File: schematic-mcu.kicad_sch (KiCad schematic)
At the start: 24 parts, among them U5 USBLC6-2P6, U6 ESP32-S3FN8, Y1 Crystal_GND24

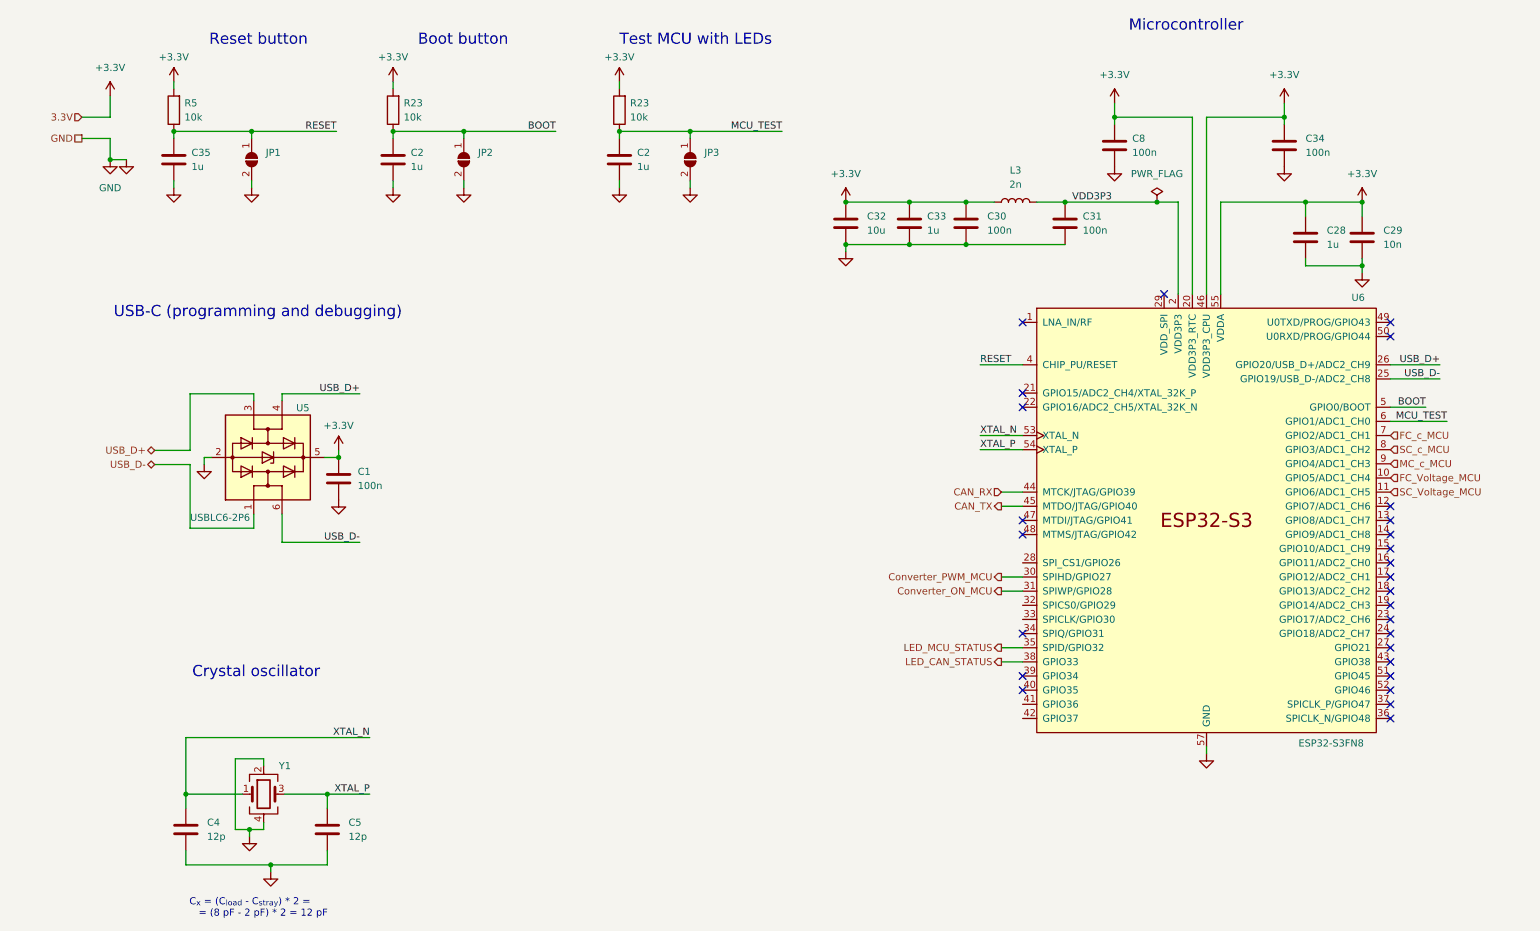
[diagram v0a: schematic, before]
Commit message: Add footprints, Placing MCU
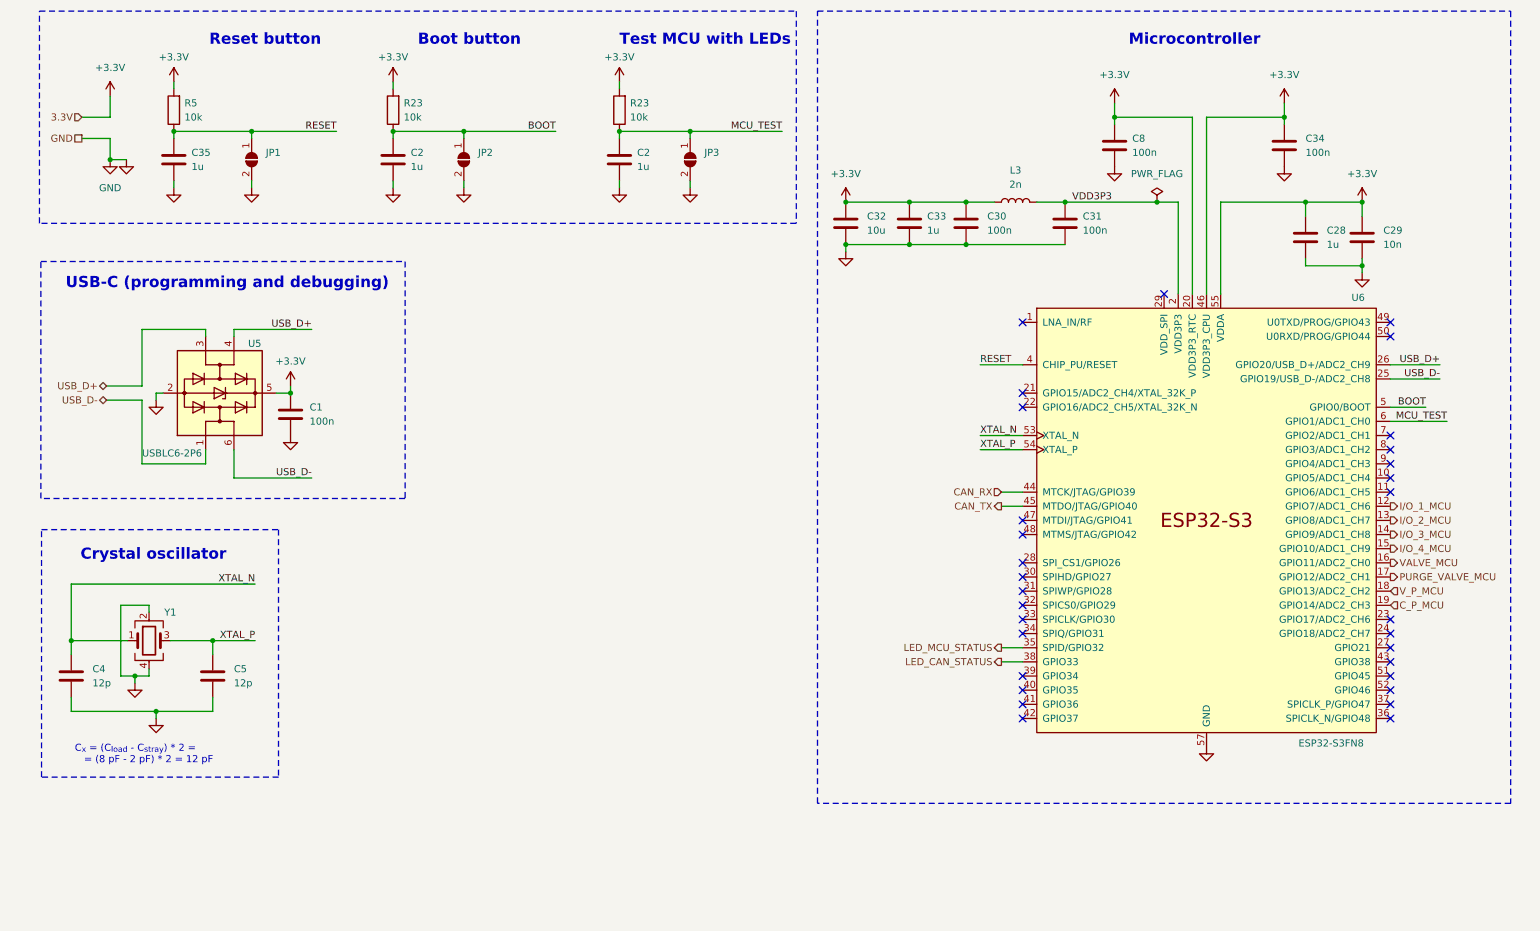
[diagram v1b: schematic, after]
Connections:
- net I/O_1_MCU: now reaches U6.12 (GPIO7/ADC1_CH6)
- net I/O_2_MCU: now reaches U6.13 (GPIO8/ADC1_CH7)
- net I/O_3_MCU: now reaches U6.14 (GPIO9/ADC1_CH8)
- net I/O_4_MCU: now reaches U6.15 (GPIO10/ADC1_CH9)
- net VALVE_MCU: now reaches U6.16 (GPIO11/ADC2_CH0)
- net PURGE_VALVE_MCU: now reaches U6.17 (GPIO12/ADC2_CH1)
- net V_P_MCU: now reaches U6.18 (GPIO13/ADC2_CH2)
- net C_P_MCU: now reaches U6.19 (GPIO14/ADC2_CH3)
- net Converter_ON_MCU: no longer names the net of U6.31 (SPIWP/GPIO28)
- net Converter_PWM_MCU: no longer names the net of U6.30 (SPIHD/GPIO27)
- net FC_Voltage_MCU: no longer names the net of U6.10 (GPIO5/ADC1_CH4)
- net FC_c_MCU: no longer names the net of U6.7 (GPIO2/ADC1_CH1)
- net MC_c_MCU: no longer names the net of U6.9 (GPIO4/ADC1_CH3)
- net SC_Voltage_MCU: no longer names the net of U6.11 (GPIO6/ADC1_CH5)
- net SC_c_MCU: no longer names the net of U6.8 (GPIO3/ADC1_CH2)
- no-connect marks 27 -> 31
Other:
- moved on the sheet: C1, C4, C5, U5, Y1

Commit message: Drawing PCB
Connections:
- net C_P_MCU: now also U6.24 (GPIO18/ADC2_CH7); no longer U6.19 (GPIO14/ADC2_CH3)
- net I/O_1_MCU: now also U6.39 (GPIO34); no longer U6.12 (GPIO7/ADC1_CH6)
- net I/O_2_MCU: now also U6.40 (GPIO35); no longer U6.13 (GPIO8/ADC1_CH7)
- net I/O_3_MCU: now also U6.41 (GPIO36); no longer U6.14 (GPIO9/ADC1_CH8)
- net I/O_4_MCU: now also U6.42 (GPIO37); no longer U6.15 (GPIO10/ADC1_CH9)
- net V_P_MCU: now also U6.23 (GPIO17/ADC2_CH6); no longer U6.18 (GPIO13/ADC2_CH2)
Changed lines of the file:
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@@
   (no_connect (at 220.98 69.85))
   (no_connect (at 195.58 90.17))
-  (no_connect (at 195.58 143.51))
+  (no_connect (at 261.62 123.19))
   (no_connect (at 261.62 95.25))
   (no_connect (at 261.62 143.51))
-  (no_connect (at 261.62 130.81))
+  (no_connect (at 261.62 125.73))
   (no_connect (at 195.58 125.73))
   (no_connect (at 195.58 74.93))
+  (no_connect (at 261.62 115.57))
   (no_connect (at 195.58 128.27))
-  (no_connect (at 195.58 138.43))
   (no_connect (at 261.62 100.33))
   (no_connect (at 195.58 87.63))
@@
   (no_connect (at 195.58 130.81))
   (no_connect (at 195.58 113.03))
-  (no_connect (at 195.58 140.97))
   (no_connect (at 261.62 102.87))
   (no_connect (at 261.62 74.93))
+  (no_connect (at 261.62 107.95))
   (no_connect (at 195.58 118.11))
-  (no_connect (at 261.62 128.27))
+  (no_connect (at 261.62 113.03))
   (no_connect (at 261.62 133.35))
   (no_connect (at 261.62 138.43))
@@
   (no_connect (at 195.58 110.49))
   (no_connect (at 261.62 135.89))
+  (no_connect (at 261.62 110.49))
   (no_connect (at 261.62 97.79))
-  (no_connect (at 195.58 146.05))
   (wire (pts (xy 163.83 62.23) (xy 163.83 60.96))
     (stroke (width 0) (type default))
@@
     (effects (font (size 1.27 1.27)) (justify right))
   )
-  (hierarchical_label "V_P_MCU" (shape input) (at 261.62 123.19 0) (fields_autoplaced)
-    (effects (font (size 1.27 1.27)) (justify left))
-  )
   (hierarchical_label "3.3V" (shape input) (at 26.67 38.1 180) (fields_autoplaced)
     (effects (font (size 1.27 1.27)) (justify right))
@@
     (effects (font (size 1.27 1.27)) (justify right))
   )
-  (hierarchical_label "I{slash}O_2_MCU" (shape output) (at 261.62 110.49 0) (fields_autoplaced)
-    (effects (font (size 1.27 1.27)) (justify left))
-  )
   (hierarchical_label "GND" (shape passive) (at 26.67 41.91 180) (fields_autoplaced)
     (effects (font (size 1.27 1.27)) (justify right))
   )
-  (hierarchical_label "I{slash}O_4_MCU" (shape output) (at 261.62 115.57 0) (fields_autoplaced)
-    (effects (font (size 1.27 1.27)) (justify left))
-  )
-  (hierarchical_label "I{slash}O_1_MCU" (shape output) (at 261.62 107.95 0) (fields_autoplaced)
-    (effects (font (size 1.27 1.27)) (justify left))
+  (hierarchical_label "I{slash}O_3_MCU" (shape output) (at 195.58 143.51 180) (fields_autoplaced)
+    (effects (font (size 1.27 1.27)) (justify right))
   )
   (hierarchical_label "VALVE_MCU" (shape output) (at 261.62 118.11 0) (fields_autoplaced)
     (effects (font (size 1.27 1.27)) (justify left))
   )
-  (hierarchical_label "I{slash}O_3_MCU" (shape output) (at 261.62 113.03 0) (fields_autoplaced)
+  (hierarchical_label "I{slash}O_1_MCU" (shape output) (at 195.58 138.43 180) (fields_autoplaced)
+    (effects (font (size 1.27 1.27)) (justify right))
+  )
+  (hierarchical_label "I{slash}O_2_MCU" (shape output) (at 195.58 140.97 180) (fields_autoplaced)
+    (effects (font (size 1.27 1.27)) (justify right))
+  )
+  (hierarchical_label "C_P_MCU" (shape input) (at 261.62 130.81 0) (fields_autoplaced)
     (effects (font (size 1.27 1.27)) (justify left))
   )
@@
     (effects (font (size 1.27 1.27)) (justify left))
   )
-  (hierarchical_label "C_P_MCU" (shape input) (at 261.62 125.73 0) (fields_autoplaced)
+  (hierarchical_label "I{slash}O_4_MCU" (shape output) (at 195.58 146.05 180) (fields_autoplaced)
+    (effects (font (size 1.27 1.27)) (justify right))
+  )
+  (hierarchical_label "V_P_MCU" (shape input) (at 261.62 128.27 0) (fields_autoplaced)
     (effects (font (size 1.27 1.27)) (justify left))
   )

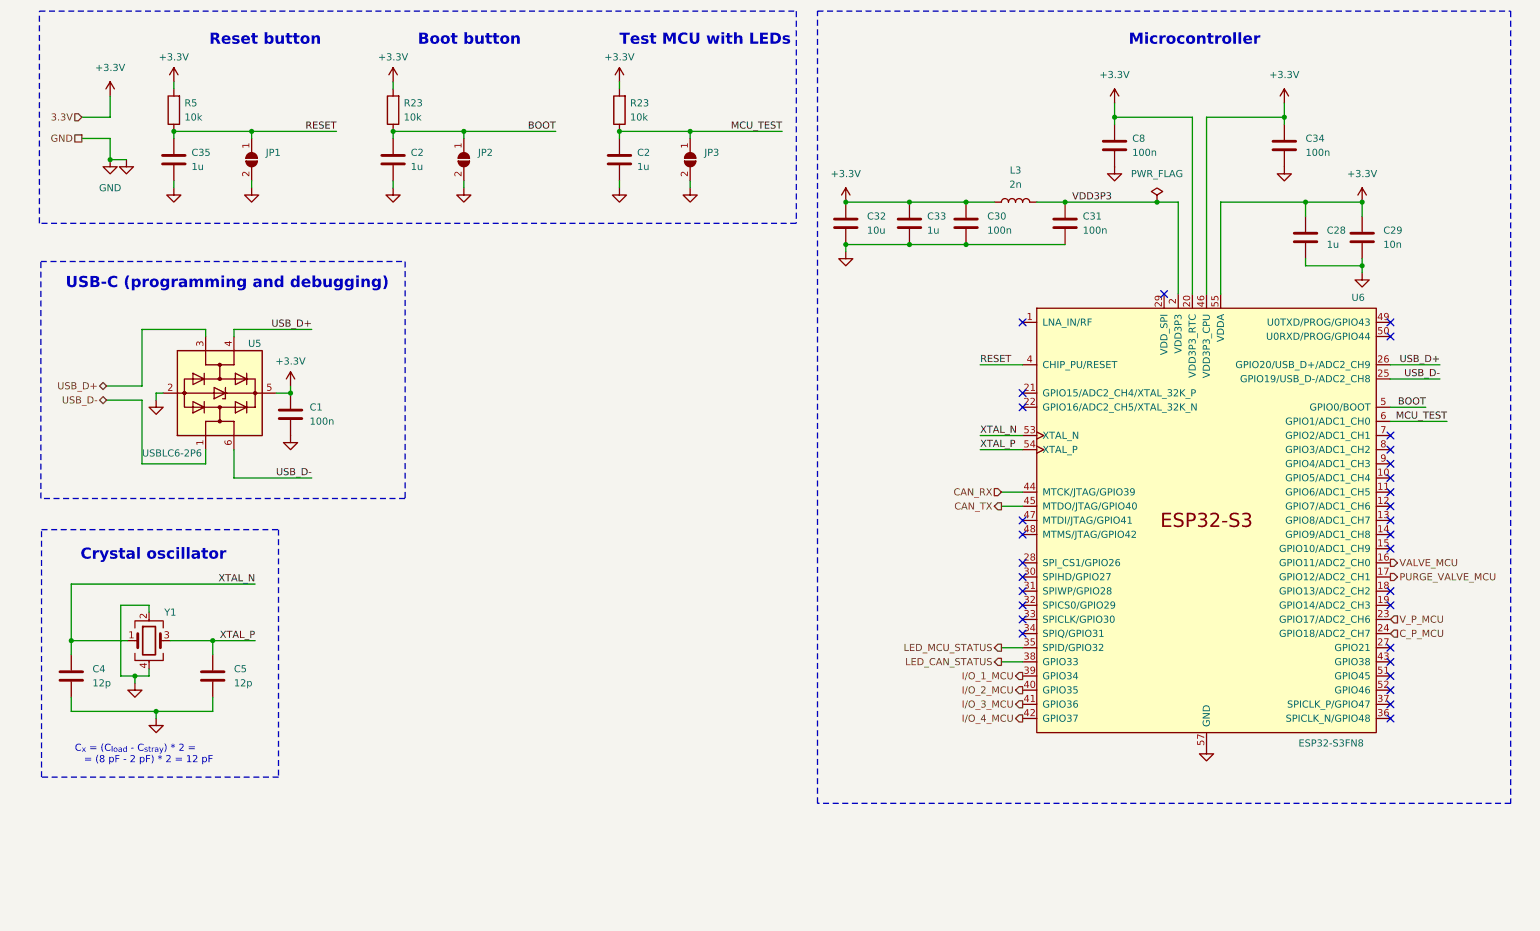
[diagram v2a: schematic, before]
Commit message: Adding connector for Hydrogen Sensor
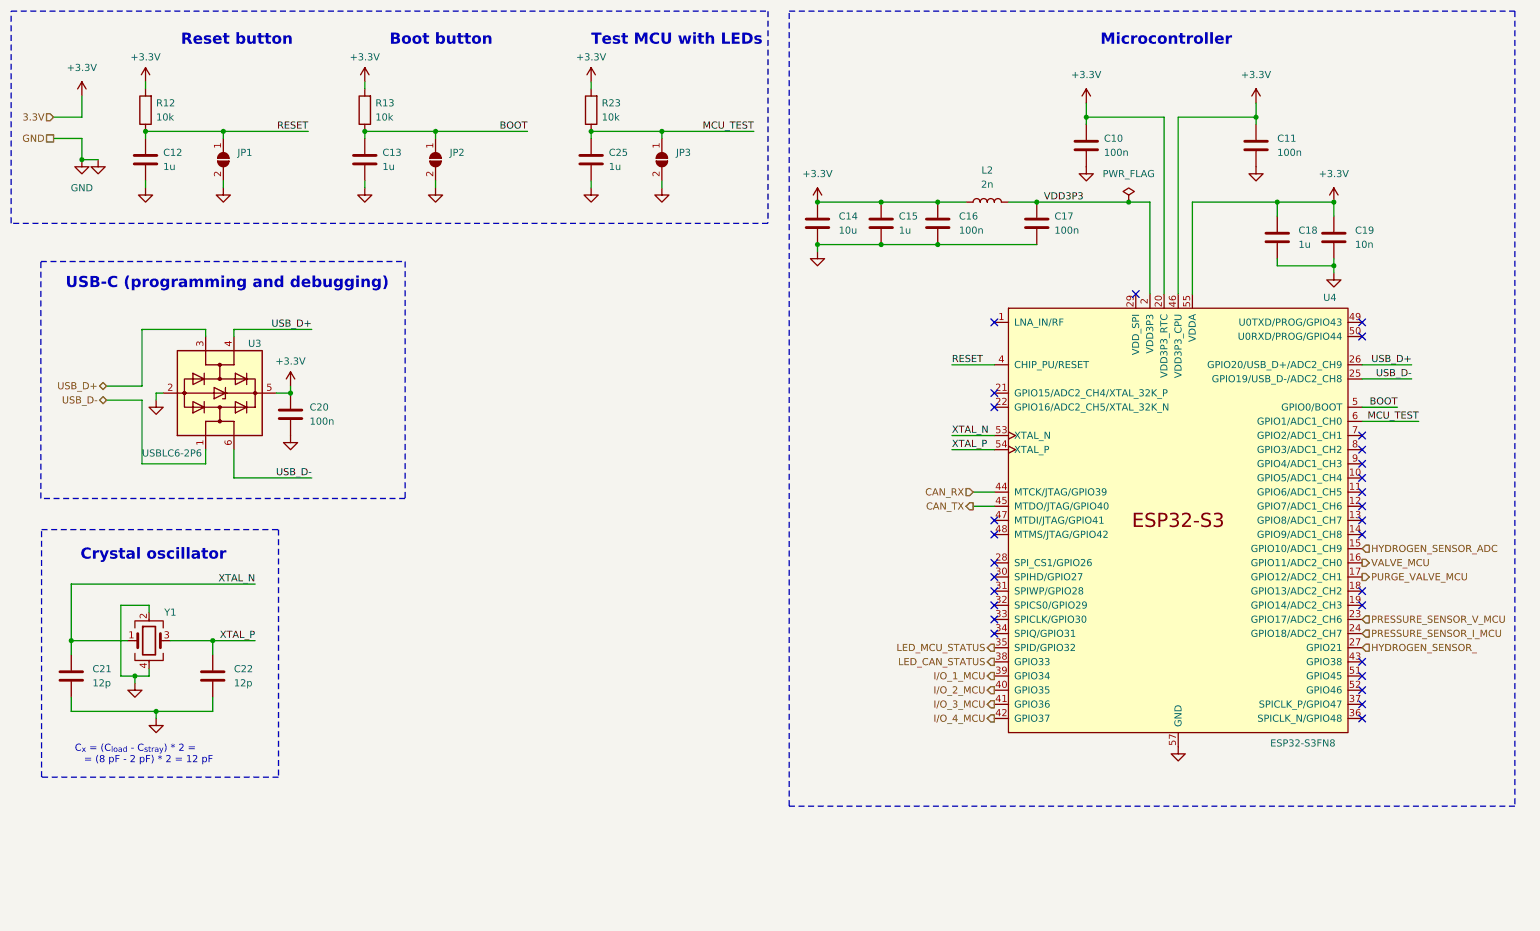
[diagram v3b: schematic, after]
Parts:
- renumbered C8 to C10, C34 to C11, C35 to C12, C2 to C13, C32 to C14, C33 to C15, C30 to C16, C31 to C17, C28 to C18, C29 to C19, C1 to C20, C4 to C21, C5 to C22, C2 to C25, L3 to L2, R5 to R12, R23 to R13, U5 to U3, U6 to U4
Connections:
- net HYDROGEN_SENSOR_ADC: now reaches U4.15 (GPIO10/ADC1_CH9)
- net HYDROGEN_SENSOR_: now reaches U4.27 (GPIO21)
- net C_P_MCU renamed PRESSURE_SENSOR_I_MCU
- net V_P_MCU renamed PRESSURE_SENSOR_V_MCU
- no-connect marks 31 -> 29
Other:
- moved on the sheet: C10, C11, C12, C13, C14, C15, C16, C17, C18, C19, C25, JP1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

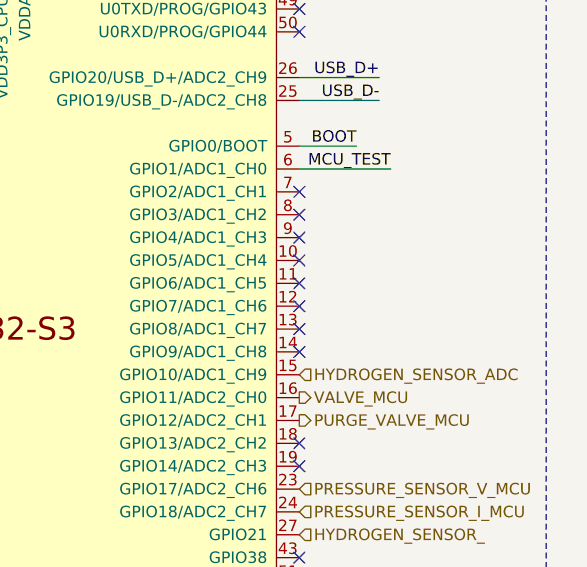
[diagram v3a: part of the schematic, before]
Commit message: Adding motor driver unit
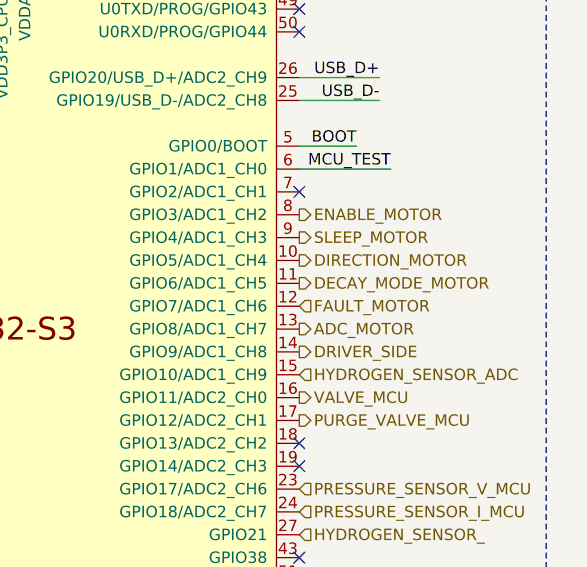
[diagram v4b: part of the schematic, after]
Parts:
- R23: footprint LED_SMD:LED_1206_3216Metric -> Resistor_SMD:R_1206_3216Metric
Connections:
- net DIRECTION_MOTOR: now reaches U4.10 (GPIO5/ADC1_CH4)
- net DECAY_MODE_MOTOR: now reaches U4.11 (GPIO6/ADC1_CH5)
- net FAULT_MOTOR: now reaches U4.12 (GPIO7/ADC1_CH6)
- net ADC_MOTOR: now reaches U4.13 (GPIO8/ADC1_CH7)
- net DRIVER_SIDE: now reaches U4.14 (GPIO9/ADC1_CH8)
- net ENABLE_MOTOR: now reaches U4.8 (GPIO3/ADC1_CH2)
- net SLEEP_MOTOR: now reaches U4.9 (GPIO4/ADC1_CH3)
- no-connect marks 29 -> 22
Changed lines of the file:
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@@
-	)
-	(no_connect
-		(at 256.54 105.41)
 	)
 	(no_connect
@@
 	)
 	(no_connect
-		(at 256.54 100.33)
-	)
-	(no_connect
 		(at 190.5 87.63)
 	)
@@
 	)
 	(no_connect
-		(at 256.54 102.87)
-	)
-	(no_connect
 		(at 256.54 74.93)
-	)
-	(no_connect
-		(at 256.54 107.95)
 	)
 	(no_connect
@@
 	)
 	(no_connect
-		(at 256.54 113.03)
-	)
-	(no_connect
 		(at 256.54 138.43)
 	)
@@
 	(no_connect
 		(at 256.54 135.89)
-	)
-	(no_connect
-		(at 256.54 110.49)
-	)
-	(no_connect
-		(at 256.54 97.79)
 	)
 	(wire
@@
 		)
 	)
+	(hierarchical_label "ENABLE_MOTOR"
+		(shape output)
+		(at 256.54 97.79 0)
+		(fields_autoplaced yes)
+		(effects
+			(font
+				(size 1.27 1.27)
+			)
+			(justify left)
+		)
+	)
 	(hierarchical_label "LED_MCU_STATUS"
 		(shape output)
@@
 		)
 	)
+	(hierarchical_label "SLEEP_MOTOR"
+		(shape output)
+		(at 256.54 100.33 0)
+		(fields_autoplaced yes)
+		(effects
+			(font
+				(size 1.27 1.27)
+			)
+			(justify left)
+		)
+	)
 	(hierarchical_label "CAN_RX"
 		(shape input)
@@
 		)
 	)
+	(hierarchical_label "FAULT_MOTOR"
+		(shape input)
+		(at 256.54 107.95 0)
+		(fields_autoplaced yes)
+		(effects
+			(font
+				(size 1.27 1.27)
+			)
+			(justify left)
+		)
+	)
+	(hierarchical_label "DECAY_MODE_MOTOR"
+		(shape output)
+		(at 256.54 105.41 0)
+		(fields_autoplaced yes)
+		(effects
+			(font
+				(size 1.27 1.27)
+			)
+			(justify left)
+		)
+	)
 	(hierarchical_label "GND"
 		(shape passive)
@@
 		)
 	)
+	(hierarchical_label "DIRECTION_MOTOR"
+		(shape output)
+		(at 256.54 102.87 0)
+		(fields_autoplaced yes)
+		(effects
+			(font
+				(size 1.27 1.27)
+			)
+			(justify left)
+		)
+	)
 	(hierarchical_label "PRESSURE_SENSOR_V_MCU"
 		(shape input)
@@
 		)
 	)
+	(hierarchical_label "ADC_MOTOR"
+		(shape output)
+		(at 256.54 110.49 0)
+		(fields_autoplaced yes)
+		(effects
+			(font
+				(size 1.27 1.27)
+			)
+			(justify left)
+		)
+	)
 	(hierarchical_label "USB_D+"
 		(shape bidirectional)
@@
 			)
 			(justify right)
+		)
+	)
+	(hierarchical_label "DRIVER_SIDE"
+		(shape output)
+		(at 256.54 113.03 0)
+		(fields_autoplaced yes)
+		(effects
+			(font
+				(size 1.27 1.27)
+			)
+			(justify left)
 		)
 	)
@@
 			)
 		)
-		(property "Footprint" "LED_SMD:LED_1206_3216Metric"
+		(property "Footprint" "Resistor_SMD:R_1206_3216Metric"
 			(at 119.888 36.83 90)
 			(effects

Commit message: Change of dimensions
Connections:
- net PRESSURE_SENSOR_I_MCU: now also U4.23 (GPIO17/ADC2_CH6); no longer U4.24 (GPIO18/ADC2_CH7)
- net PRESSURE_SENSOR_V_MCU: now also U4.24 (GPIO18/ADC2_CH7); no longer U4.23 (GPIO17/ADC2_CH6)
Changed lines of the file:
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@@
 	(hierarchical_label "PRESSURE_SENSOR_I_MCU"
 		(shape input)
-		(at 256.54 130.81 0)
+		(at 256.54 128.27 0)
 		(fields_autoplaced yes)
 		(effects
@@
 	(hierarchical_label "PRESSURE_SENSOR_V_MCU"
 		(shape input)
-		(at 256.54 128.27 0)
+		(at 256.54 130.81 0)
 		(fields_autoplaced yes)
 		(effects
